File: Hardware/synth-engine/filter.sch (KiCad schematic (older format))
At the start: 1 part

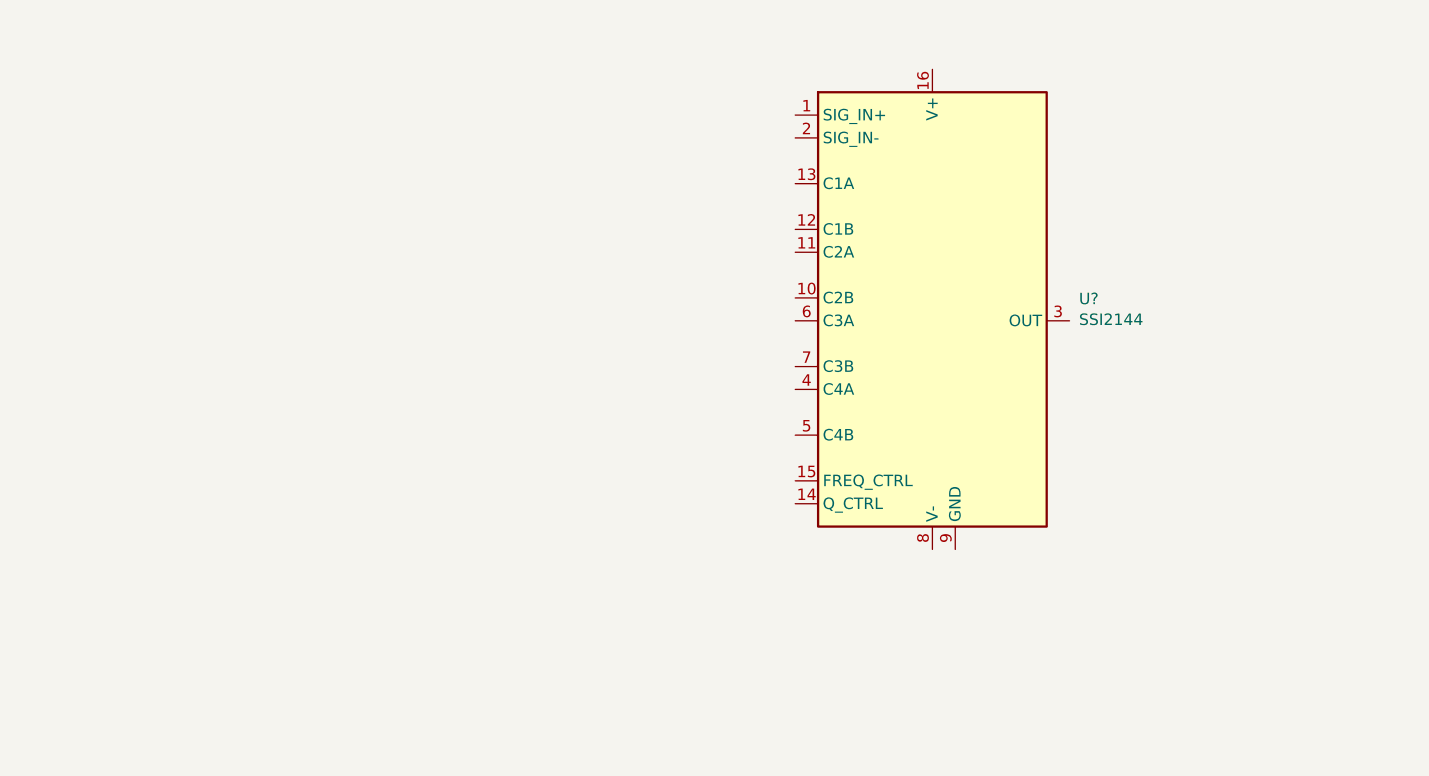
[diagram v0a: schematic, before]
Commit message: add SSI2144 implementation * basically default datasheet version
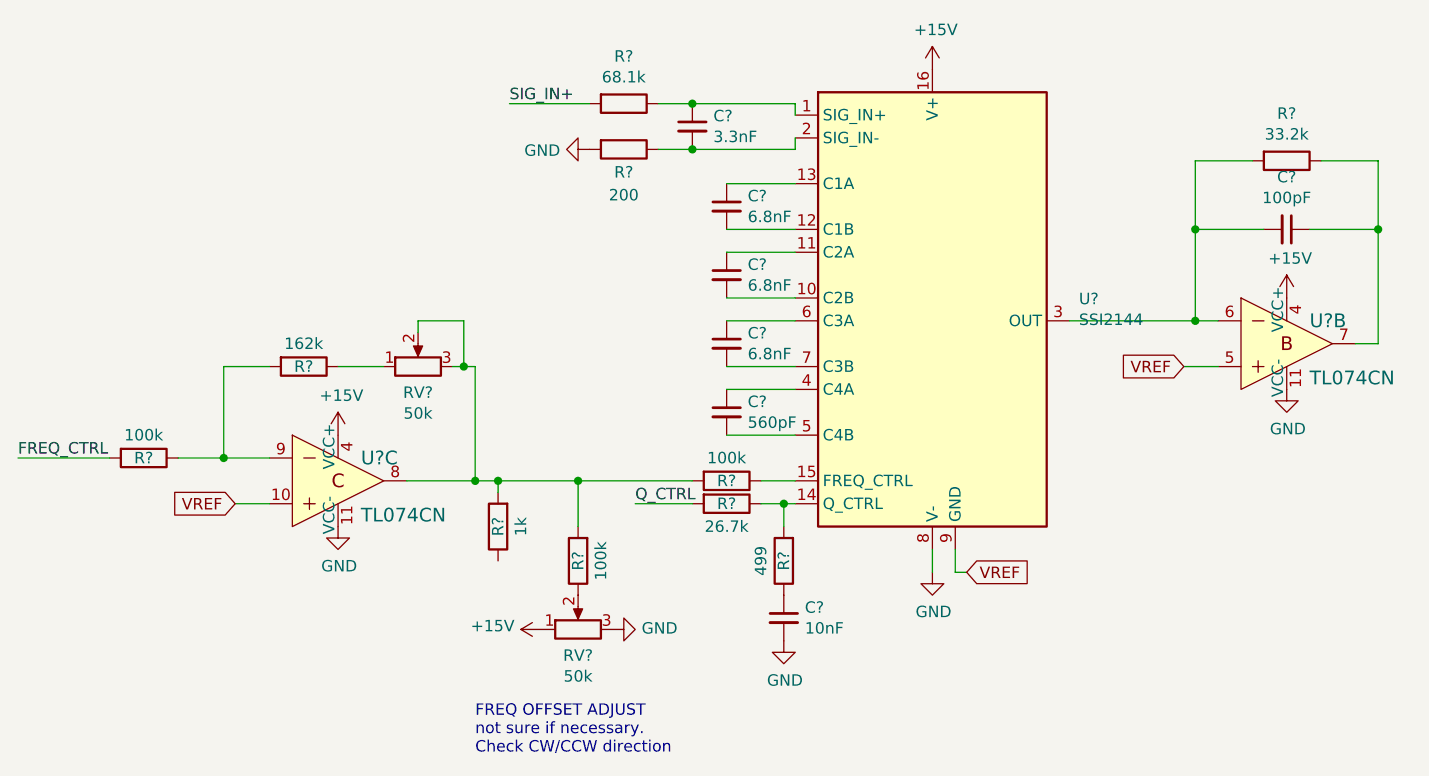
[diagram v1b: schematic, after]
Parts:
- added C?: 3.3nF, symbol Device:C_Small
- added C?: 560pF, symbol Device:C_Small
- added C? (x3): 6.8nF, symbol Device:C_Small
- added C?: 100pF, symbol Device:C_Small
- added C?: 10nF, symbol Device:C_Small
- added R?: 68.1k, symbol Device:R
- added R?: 200, symbol Device:R
- added R?: 33.2k, symbol Device:R
- added R?: 26.7k, symbol Device:R
- added R? (x3): 100k, symbol Device:R
- added R?: 162k, symbol Device:R
- added R?: 1k, symbol Device:R
- added R?: 499, symbol Device:R
- added RV? (x2): 50k, symbol Device:R_POT
- added U? (x2): TL074CN, digikey-footprints:DIP-14_W3mm, symbol dk_Linear-Amplifiers-Instrumentation-OP-Amps-Buffer-Amps:TL074CN
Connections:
- net at U?.1 (SIG_IN+): now also C?.1, R?.1
- net at U?.10 (C2B): now also C?.2
- net at U?.11 (C2A): now also C?.1
- net at U?.12 (C1B): now also C?.2
- net at U?.13 (C1A): now also C?.1
- net at U?.14 (Q_CTRL): now also R?.1, R?.2
- net at U?.15 (FREQ_CTRL): now also R?.1
- net +15V: now reaches U?.16 (V+)
- net +15V: now also RV?.1, U?.4 (VCC+), U?.4 (VCC+)
- net at U?.2 (SIG_IN-): now also C?.2, R?.1
- net at U?.3 (OUT): now also C?.2, R?.2, U?.6
- net at U?.4 (C4A): now also C?.1
- net at U?.5 (C4B): now also C?.2
- net at U?.6 (C3A): now also C?.1
- net at U?.7 (C3B): now also C?.2
- net GND: now reaches U?.8 (V-)
- net GND: now also C?.2, R?.2, RV?.3, U?.11 (VCC-), U?.11 (VCC-)
- net VREF: now reaches U?.9 (GND)
- net VREF: now also U?.10, U?.5
- new net: C?.1, R?.1, U?.7
- new net: R?.2, R?.2, R?.2, RV?.2, RV?.3, U?.8
- new net: R?.1, R?.2, U?.9
- new net: R?.1, RV?.2
- new net: R?.1, RV?.1
- new net: C?.1, R?.1
- new net FREQ_CTRL: R?.2
- new net Q_CTRL: R?.2
- new net SIG_IN+: R?.2
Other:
- note added: "FREQ OFFSET ADJUST\nnot sure if necessary.\nCheck CW/CCW direction"

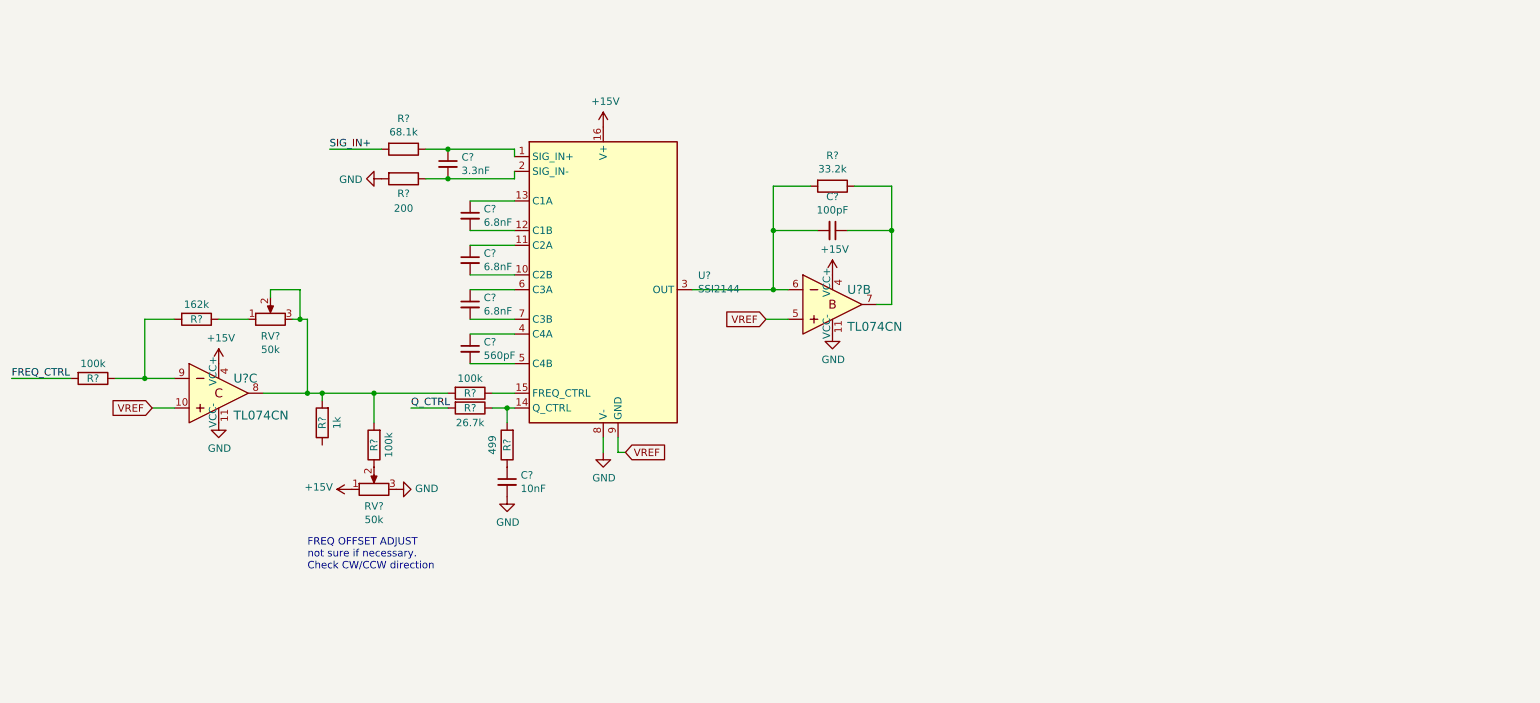
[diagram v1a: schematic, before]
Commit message: fix some ground/VREF mixups on filter schematic
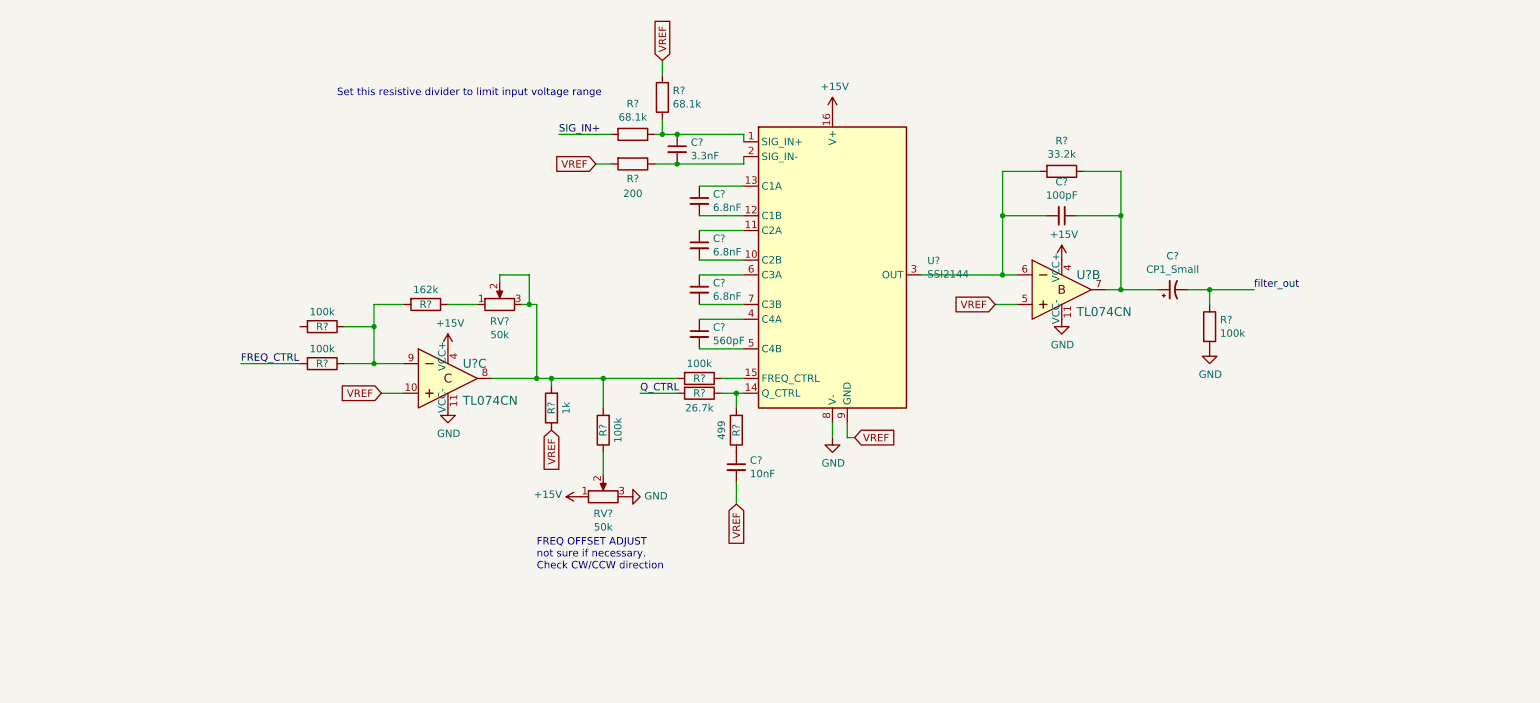
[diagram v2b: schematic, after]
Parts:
- added C?: CP1_Small, symbol Device:CP1_Small
- added R?: 68.1k, symbol Device:R
- added R? (x2): 100k, symbol Device:R
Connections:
- net GND: now also R?.2; no longer C?.2, R?.2
- net VREF: now also C?.2, R?.1, R?.2, R?.2
- net at C?.1, R?.1, U?.1 (SIG_IN+): now also R?.1
- net at C?.1, R?.1, U?.7: now also C?.1
- net at R?.1, R?.2, U?.9: now also R?.1
- new net filter_out: C?.2, R?.1
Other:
- note added: "Set this resistive divider to limit input voltage range"
- moved on the sheet: C?, R?, RV?, U?, U?B, U?C

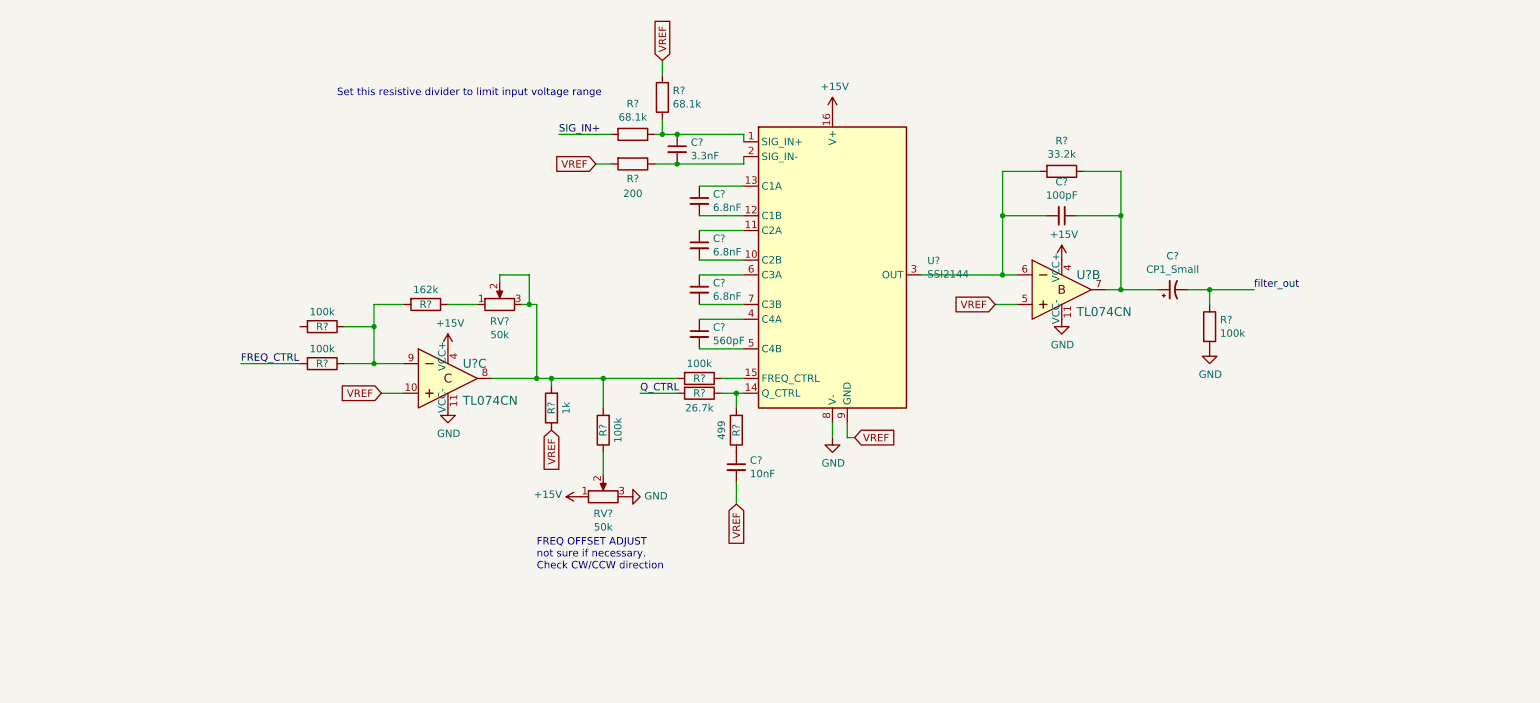
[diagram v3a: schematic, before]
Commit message: add filter potentiometers I believe filter is finalized now.
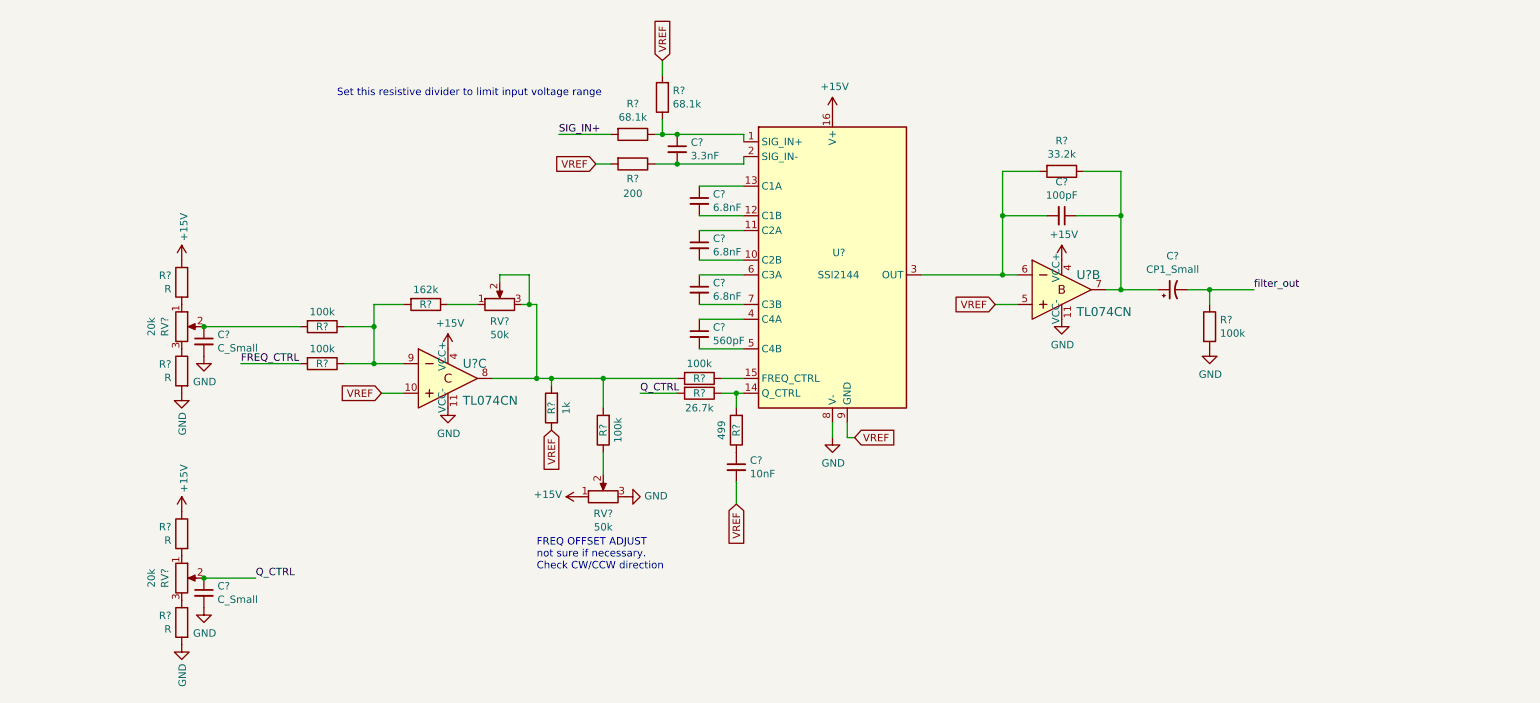
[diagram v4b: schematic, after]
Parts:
- added C? (x2): C_Small, symbol Device:C_Small
- added R? (x4): R, symbol Device:R
- added RV? (x2): 20k, symbol Device:R_POT
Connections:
- net +15V: now also R?.1, R?.1
- net GND: now also C?.2, C?.2, R?.2, R?.2
- net Q_CTRL: now also C?.1, RV?.2
- net at R?.2: now also C?.1, RV?.2
- new net: R?.2, RV?.1 (x2)
- new net: R?.1, RV?.3 (x2)
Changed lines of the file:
@@
 U 1 1 5DDC7EE1
 P 6400 3600
-F 0 "U?" H 7041 3696 50  0000 L CNN
-F 1 "SSI2144" H 7041 3605 50  0000 L CNN
+F 0 "U?" H 6400 3750 50  0000 L CNN
+F 1 "SSI2144" H 6300 3600 50  0000 L CNN
 F 2 "Package_SO:SSOP-16_3.9x4.9mm_P0.635mm" H 7300 3500 50  0001 C CNN
 F 3 "http://www.soundsemiconductor.com/downloads/ssi2144datasheet.pdf" H 7100 3350 50  0001 C CNN
@@
 Text Label 9250 3700 0    50   ~ 0
 filter_out
+$Comp
+L power:+15V #PWR?
+U 1 1 5DDC8B0C
+P 2000 3500
+F 0 "#PWR?" H 2000 3350 50  0001 C CNN
+F 1 "+15V" V 2015 3628 50  0000 L CNN
+F 2 "" H 2000 3500 50  0001 C CNN
+F 3 "" H 2000 3500 50  0001 C CNN
+	1    2000 3500
+	1    0    0    -1
+$EndComp
+$Comp
+L power:GND #PWR?
+U 1 1 5DDC8B12
+P 2000 4400
+F 0 "#PWR?" H 2000 4150 50  0001 C CNN
+F 1 "GND" V 2005 4272 50  0000 R CNN
+F 2 "" H 2000 4400 50  0001 C CNN
+F 3 "" H 2000 4400 50  0001 C CNN
+	1    2000 4400
+	1    0    0    -1
+$EndComp
+$Comp
+L Device:R_POT RV?
+U 1 1 5DDC8B18
+P 2000 3950
+F 0 "RV?" V 1886 3950 50  0000 C CNN
+F 1 "20k" V 1795 3950 50  0000 C CNN
+F 2 "" H 2000 3950 50  0001 C CNN
+F 3 "~" H 2000 3950 50  0001 C CNN
+	1    2000 3950
+	1    0    0    -1
+$EndComp
+Wire Wire Line
+	2150 3950 2800 3950
+$Comp
+L Device:R R?
+U 1 1 5DDD4D4F
+P 2000 4250
+F 0 "R?" H 2070 4296 50  0000 L CNN
+F 1 "R" H 2070 4205 50  0000 L CNN
+F 2 "" V 1930 4250 50  0001 C CNN
+F 3 "~" H 2000 4250 50  0001 C CNN
+	1    2000 4250
+	-1   0    0    -1
+$EndComp
+$Comp
+L Device:R R?
+U 1 1 5DDD7C21
+P 2000 3650
+F 0 "R?" H 2070 3696 50  0000 L CNN
+F 1 "R" H 2070 3605 50  0000 L CNN
+F 2 "" V 1930 3650 50  0001 C CNN
+F 3 "~" H 2000 3650 50  0001 C CNN
+	1    2000 3650
+	-1   0    0    -1
+$EndComp
+$Comp
+L Device:C_Small C?
+U 1 1 5DDDB3D4
+P 2150 4050
+F 0 "C?" H 2242 4096 50  0000 L CNN
+F 1 "C_Small" H 2242 4005 50  0000 L CNN
+F 2 "" H 2150 4050 50  0001 C CNN
+F 3 "~" H 2150 4050 50  0001 C CNN
+	1    2150 4050
+	1    0    0    -1
+$EndComp
+Connection ~ 2150 3950
+$Comp
+L power:GND #PWR?
+U 1 1 5DDDB4EF
+P 2150 4150
+F 0 "#PWR?" H 2150 3900 50  0001 C CNN
+F 1 "GND" H 2155 3977 50  0000 C CNN
+F 2 "" H 2150 4150 50  0001 C CNN
+F 3 "" H 2150 4150 50  0001 C CNN
+	1    2150 4150
+	1    0    0    -1
+$EndComp
+$Comp
+L power:+15V #PWR?
+U 1 1 5DDE1C9A
+P 2000 5200
+F 0 "#PWR?" H 2000 5050 50  0001 C CNN
+F 1 "+15V" V 2015 5328 50  0000 L CNN
+F 2 "" H 2000 5200 50  0001 C CNN
+F 3 "" H 2000 5200 50  0001 C CNN
+	1    2000 5200
+	1    0    0    -1
+$EndComp
+$Comp
+L power:GND #PWR?
+U 1 1 5DDE1CA0
+P 2000 6100
+F 0 "#PWR?" H 2000 5850 50  0001 C CNN
+F 1 "GND" V 2005 5972 50  0000 R CNN
+F 2 "" H 2000 6100 50  0001 C CNN
+F 3 "" H 2000 6100 50  0001 C CNN
+	1    2000 6100
+	1    0    0    -1
+$EndComp
+$Comp
+L Device:R_POT RV?
+U 1 1 5DDE1CA6
+P 2000 5650
+F 0 "RV?" V 1886 5650 50  0000 C CNN
+F 1 "20k" V 1795 5650 50  0000 C CNN
+F 2 "" H 2000 5650 50  0001 C CNN
+F 3 "~" H 2000 5650 50  0001 C CNN
+	1    2000 5650
+	1    0    0    -1
+$EndComp
+Wire Wire Line
+	2150 5650 2500 5650
+$Comp
+L Device:R R?
+U 1 1 5DDE1CAD
+P 2000 5950
+F 0 "R?" H 2070 5996 50  0000 L CNN
+F 1 "R" H 2070 5905 50  0000 L CNN
+F 2 "" V 1930 5950 50  0001 C CNN
+F 3 "~" H 2000 5950 50  0001 C CNN
+	1    2000 5950
+	-1   0    0    -1
+$EndComp
+$Comp
+L Device:R R?
+U 1 1 5DDE1CB3
+P 2000 5350
+F 0 "R?" H 2070 5396 50  0000 L CNN
+F 1 "R" H 2070 5305 50  0000 L CNN
+F 2 "" V 1930 5350 50  0001 C CNN
+F 3 "~" H 2000 5350 50  0001 C CNN
+	1    2000 5350
+	-1   0    0    -1
+$EndComp
+$Comp
+L Device:C_Small C?
+U 1 1 5DDE1CB9
+P 2150 5750
+F 0 "C?" H 2242 5796 50  0000 L CNN
+F 1 "C_Small" H 2242 5705 50  0000 L CNN
+F 2 "" H 2150 5750 50  0001 C CNN
+F 3 "~" H 2150 5750 50  0001 C CNN
+	1    2150 5750
+	1    0    0    -1
+$EndComp
+Connection ~ 2150 5650
+$Comp
+L power:GND #PWR?
+U 1 1 5DDE1CC0
+P 2150 5850
+F 0 "#PWR?" H 2150 5600 50  0001 C CNN
+F 1 "GND" H 2155 5677 50  0000 C CNN
+F 2 "" H 2150 5850 50  0001 C CNN
+F 3 "" H 2150 5850 50  0001 C CNN
+	1    2150 5850
+	1    0    0    -1
+$EndComp
+Text Label 2500 5650 0    50   ~ 0
+Q_CTRL
 $EndSCHEMATC
